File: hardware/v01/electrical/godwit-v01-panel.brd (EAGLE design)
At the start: 72.5 x 132.8 mm, 98 parts, among them J1 USB-MINIB-M26FTR, U1 BQ24251, U2 LM3668-3034, U3 UC530, U4 AAT4280A, U5 BMP180, U6 MAG3110, U7 ATUCL4U-TQFP48

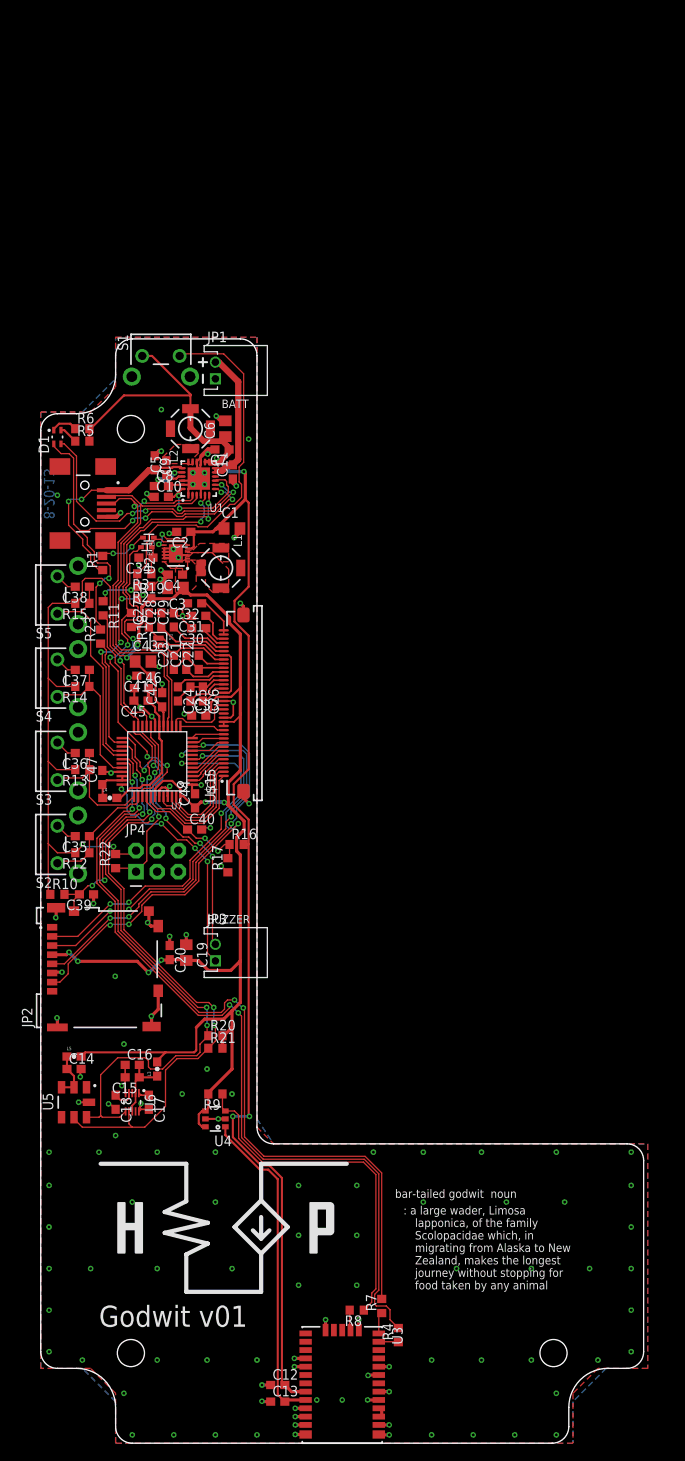
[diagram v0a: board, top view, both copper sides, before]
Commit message: panelized and gerbered.
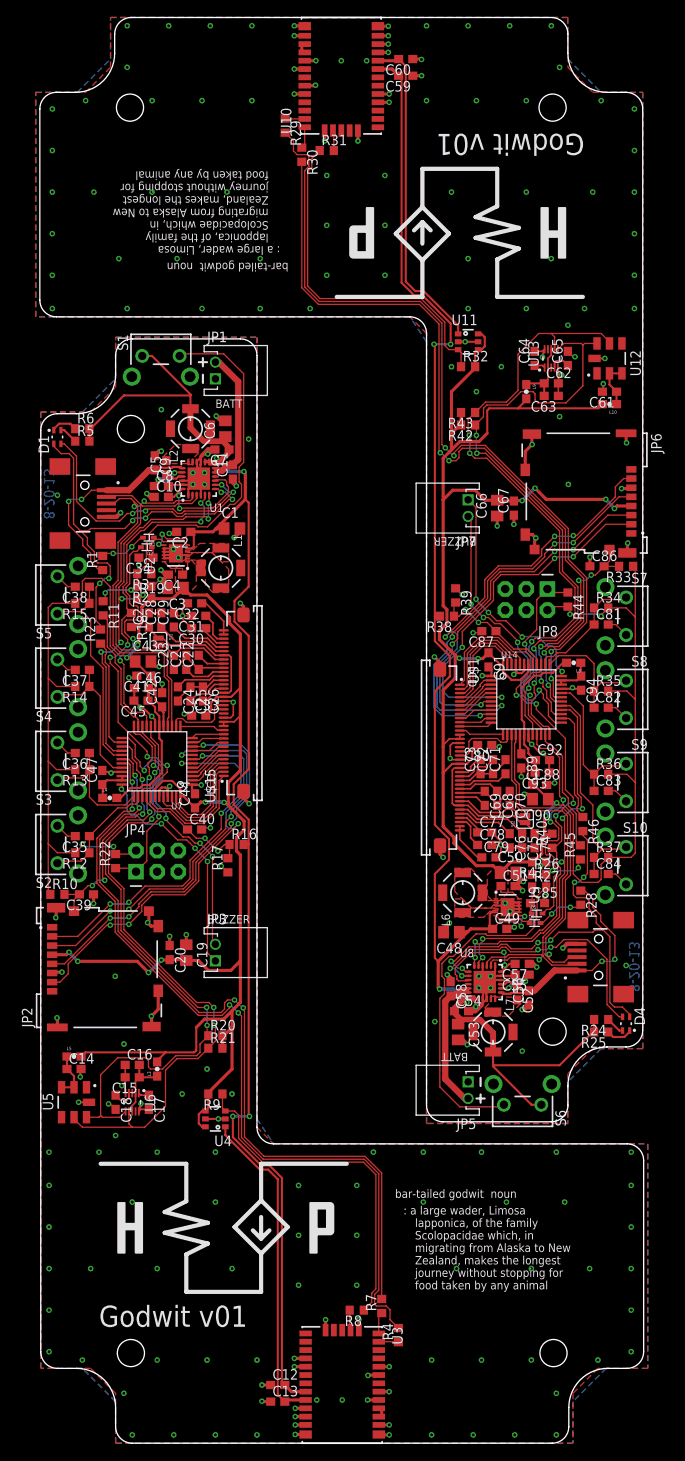
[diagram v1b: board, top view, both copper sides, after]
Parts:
- added C48, C66: 10uF, hybridpi-rcl:C0805
- added C49, C51, C54, C61, C62, C64, C65, C67, C81, C82, C83, C84, C85, C86, C87, C88, C92, C94: 0.1uF, hybridpi-rcl:C0603
- added C50, C53, C90: 22uF, hybridpi-rcl:C0805
- added C52, C89, C91: 33nF, hybridpi-rcl:C0603
- added C55, C57, C59, C63, C68, C69, C71, C72, C73, C74, C75, C76, C77, C78, C79, C80: 1uF, hybridpi-rcl:C0603
- added C56, C58, C93: 2.2uF, hybridpi-rcl:C0603
- added C60: 4.7uF, hybridpi-rcl:C0603
- added C70: DNP, hybridpi-rcl:C0603
- added D4: LED-RG-APT, hybridpi-opto:LED-2-1.6X1.25
- added D5, D6: (no value), hybridpi-discrete-semi:SOD523
- added J2: USB-MINIB-M26FTR, hybridpi-connector:USB-MINIB-M26FTR
- added JP5, JP7: M02-JST-PH-2-RA, hybridpi-connector:JST-PH-2-RA
- added JP6: MICRO-SD-5031821853, hybridpi-connector:MICROSD-5031821853
- added JP8: (no value), hybridpi-connector:2X3-NS
- added L10, L8, L9: 2.5K, hybridpi:0603
- added L6: 2.2uH, hybridpi:SRU5028
- added L7: 1uH, hybridpi:SRU5028
- added R24, R25, R26: 2.2K, hybridpi-rcl:R0603
- added R27, R28, R32, R33, R34, R35, R36, R37, R45, R46: 100K, hybridpi-rcl:R0603
- added R29, R30, R31: 220R, hybridpi-rcl:R0603
- added R38: 59K, hybridpi-rcl:R0603
- added R39: 41.2K, hybridpi-rcl:R0603
- added R40, R41, R42, R43, R44: 10K, hybridpi-rcl:R0603
- added S10, S6, S7, S8, S9: (no value), hybridpi-electromechanical:FSMRA
- added SJ2: SOLDERJUMPERNC, hybridpi-passive:SJ_2S
- added U$1: 128240D, hybridpi-connector:128240D
- added U$2: (no value), hybridpi-aesthetics:LOGO_MED_SLK
- added U10: UC530, hybridpi-rf:UC530
- added U11: AAT4280A, hybridpi-poweric:SOT23-6
- added U12: BMP180, hybridpi-sensor:BMP180
- added U13: MAG3110, hybridpi-sensor:DFN-10-2X2
- added U14: ATUCL4U-TQFP48, hybridpi-digitalic:TQFP48
- added U8: BQ24251, hybridpi:VQFN-24
- added U9: LM3668-3034, hybridpi:WSON-12
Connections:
- new net !PG!_LED1: D4.4, U8.8
- new net !RESET!1: JP8.1, R44.1, U14.22
- new net 3.0V1: C50.1, C51.1, C66.2, C67.2, C80.2, C88.1, C89.1, C90.1, C91.1, JP6.4, JP8.2, L10.2, L9.2, R32.2, R33.1, R34.2, R35.2, R36.2, R37.2, R40.2, R41.2, R42.2, R43.2, R44.2, U$1.13, U$1.14, U$1.20, U11.4, U11.6, U14.17, U14.42, U14.48, U9.1, U9.12
- new net 3V_EN1: D5.A, U14.21
- new net B_BCK1: C84.1, R37.1, S10.3, U14.29
- new net B_DWN1: C83.1, R36.1, S9.3, U14.32
- new net B_SEL1: C82.1, R35.1, S8.3, U14.37
- new net B_UP1: C81.1, R34.1, S7.3, U14.38
- new net CHRG_SCL1: R41.1, U14.28, U8.6
- new net CHRG_SDA1: R40.1, U14.39, U8.5
- new net CHRG_STAT1: R46.1, U14.26
- new net GND1: C48.2, C49.2, C50.2, C51.2, C53.2, C54.2, C55.2, C56.1, C57.1, C58.1, C59.1, C60.1, C61.2, C62.2, C63.1, C64.2, C65.2, C66.1, C67.1, C74.2, C75.2, C76.2, C77.2, C78.2, C79.2, C80.1, C81.2, C82.2, C83.2, C84.2, C85.2, C86.1, C87.2, C88.2, C89.2, C90.2, C91.2, C92.2, C93.1, C94.2, J2.5, JP5.1, JP6.6, JP6.CRD_DETL, JP6.SHIELD1, JP6.SHIELD2, JP6.SHIELD3, JP6.SHIELD4, JP6.SHIELD5, JP8.6, R26.1, R39.1, S10.1, S7.1, S8.1, S9.1, U$1.15, U$1.19, U$1.SHIELD1, U$1.SHIELD2, U10.10, U10.11, U10.12, U10.13, U10.14, U10.15, U10.18, U10.19, U10.21, U10.22, U10.27, U10.31, U10.4, U10.5, U11.2, U11.5, U12.7, U13.10, U13.5, U14.1, U14.19, U14.33, U14.43, U14.45, U8.1, U8.15, U8.16, U8.22, U8.23, U8.4, U8.PAD, U9.10, U9.11, U9.3, U9.8, U9.9, U9.PAD
- new net GPS_RX1: R30.2, U14.30
- new net GPS_TX1: R29.2, U14.31
- new net LCD_!CS!1: U$1.18, U14.14
- new net LCD_!RST!1: U$1.12, U14.13
- new net LCD_A1: U$1.1, U14.41
- new net LCD_D10: U$1.8, U14.5
- new net LCD_D11: U$1.7, U14.4
- new net LCD_D12: U$1.6, U14.3
- new net LCD_D13: U$1.4, U14.47
- new net LCD_D14: U$1.3, U14.46
- new net LCD_D15: U$1.5, U14.2
- new net LCD_D8: U$1.10, U14.11
- new net LCD_D9: U$1.9, U14.9
- new net LCD_RD1: U$1.11, U14.12
- new net LCD_WR1: U$1.2, U14.44
- new net LDO1: C57.2, U8.24, U8.9
- new net N$100: C76.1, U$1.32
- new net N$101: C77.1, U$1.33
- new net N$102: C78.1, U$1.34
- new net N$103: C79.1, U$1.35, U$1.36
- new net N$104: U$1.17
- new net N$105: U$1.16
- new net N$106: C87.1, R38.1, R39.2, U14.40
- new net N$107: JP7.1, U14.36
- new net N$108: JP7.2, U14.25
- new net N$109: C92.1, C93.2, L8.2, U14.18
- new net N$110: C94.1, L8.1, U14.34, U14.35
- new net N$111: C61.1, L10.1, U12.2, U12.3
- new net N$112: C62.1, C63.2, L9.1, U13.2, U13.8
- new net N$113: JP8.3
- new net N$114: JP8.5
- new net N$115: JP8.4
- new net N$116: R26.2, R27.2, R45.1, S6.1
- new net N$58: L6.2, U9.2
- new net N$59: L6.1, U9.4
- new net N$60: C52.1, U8.21
- new net N$61: C52.2, L7.1, U8.17, U8.18
- new net N$62: C55.1, U8.20
- new net N$63: D4.3, R24.1
- new net N$64: D4.1, R25.1
- new net N$65: U8.10
- new net N$66: D6.A, R28.2
- new net N$67: C85.1, D5.C, D6.C, R27.1, U9.6
- new net N$68: U10.16, U10.17
- new net N$69: U10.3
- new net N$70: U10.6
- new net N$71: U10.29
- new net N$72: U10.7
- new net N$73: U10.1
- new net N$74: U10.20
- new net N$75: U10.24
- new net N$76: U10.2
- new net N$77: U10.23
- new net N$78: U10.30
- new net N$79: C60.2, U10.9, U11.1
- new net N$80: R29.1, U10.25
- new net N$81: R30.1, U10.26
- new net N$82: R31.2, U10.28
- new net N$83: R31.1, R32.1, U11.3
- new net N$84: C65.1, U13.4
- new net N$85: C64.1, U13.1
- new net N$86: U13.9
- new net N$87: JP6.1
- new net N$89: JP6.8
- new net N$90: C68.2, C69.1, C70.1, U$1.27
- new net N$91: C68.1, U$1.26
- new net N$92: C69.2, U$1.28
- new net N$93: C70.2, SJ2.2, U$1.29
- new net N$94: C71.2, C72.1, C73.1, U$1.24
- new net N$95: C71.1, U$1.25
- new net N$96: C72.2, U$1.23
- new net N$97: C73.2, U$1.22
- new net N$98: C74.1, SJ2.1, U$1.21, U$1.30
- new net N$99: C75.1, U$1.31
- new net PWR_TACT1: R45.2, U14.23
- new net SD_!CS!1: JP6.2, U14.6
- new net SD_CRD_DET1: C86.2, JP6.CRD_DETH, R33.2, U14.27
- new net SD_MISO1: JP6.7, U14.7
- new net SD_MOSI1: JP6.3, U14.8
- new net SD_SCLK1: JP6.5, U14.10
- new net SENS_SCL1: R43.1, U12.5, U13.7, U14.20
- new net SENS_SDA1: R42.1, U12.6, U13.6, U14.24
- new net STAT_LED1: D4.2, R46.2, U8.7
- new net USB_D+1: J2.3, U14.16, U8.2
- new net USB_D-1: J2.2, U14.15, U8.3
- new net VBUS1: C56.2, J2.1, R28.1, U8.19
- new net VSYS1: C48.1, C49.1, C53.1, C54.1, C59.2, L7.2, R24.2, R25.2, R38.2, S6.3, U10.8, U8.13, U8.14, U9.5, U9.7
- new net V_BATT1: C58.2, JP5.2, U8.11, U8.12
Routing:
- net 3.0V1: track 0.00 -> 252.4 mm, vias 0 -> 10
- net VSYS1: track 0.00 -> 181.8 mm, vias 0 -> 6
- net GND1: track 0.00 -> 136.0 mm, vias 0 -> 127
- net GPS_TX1: track 0.00 -> 98.5 mm, vias 0 -> 4
- net GPS_RX1: track 0.00 -> 95.1 mm, vias 0 -> 4
- net SENS_SCL1: track 0.00 -> 75.2 mm, vias 0 -> 4
- net SENS_SDA1: track 0.00 -> 75.1 mm, vias 0 -> 4
- net CHRG_SDA1: track 0.00 -> 52.1 mm, vias 0 -> 6
- net STAT_LED1: track 0.00 -> 50.4 mm, vias 0 -> 6
- net SD_MISO1: track 0.00 -> 50.0 mm, vias 0 -> 4
- net N$116: track 0.00 -> 49.3 mm, vias 0 -> 2
- net SD_MOSI1: track 0.00 -> 47.4 mm, vias 0 -> 4
- net CHRG_SCL1: track 0.00 -> 47.1 mm, vias 0 -> 6
- net SD_SCLK1: track 0.00 -> 47.0 mm, vias 0 -> 4
- net USB_D+1: track 0.00 -> 46.4 mm, vias 0 -> 2
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- added copper zone on layer 1, net 3.0V1
- added copper zone on layer 1, net GND1
- added copper zone on layer 16, net GND1
- added copper zone on layer 1, net N$58
- added copper zone on layer 1, net N$59
- added copper zone on layer 1, net N$61
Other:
- board size 72.5 x 132.8 mm -> 72.6 x 171.4 mm
